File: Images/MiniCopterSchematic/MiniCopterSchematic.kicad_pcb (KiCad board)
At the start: 2 copper layers, 78.6 x 58.6 mm, 53 parts, among them J1 MPU6050, M1 Motor_DC_1, M2 Motor_DC_2, M3 Motor_DC_3, M4 Motor_DC_4, Q1 FQP20NO6L, Q2 FQP20NO6L, Q3 FQP20NO6L, Q4 FQP20NO6L

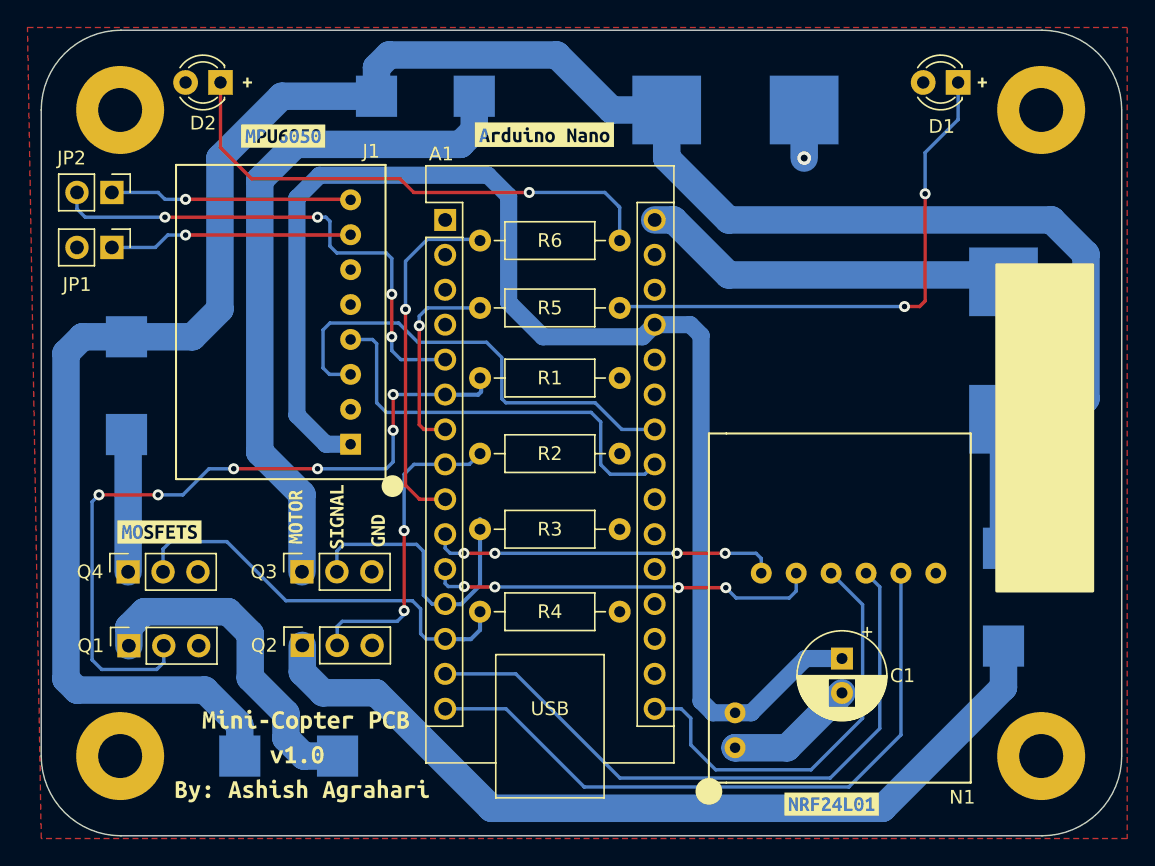
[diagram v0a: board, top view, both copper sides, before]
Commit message: Updated labels
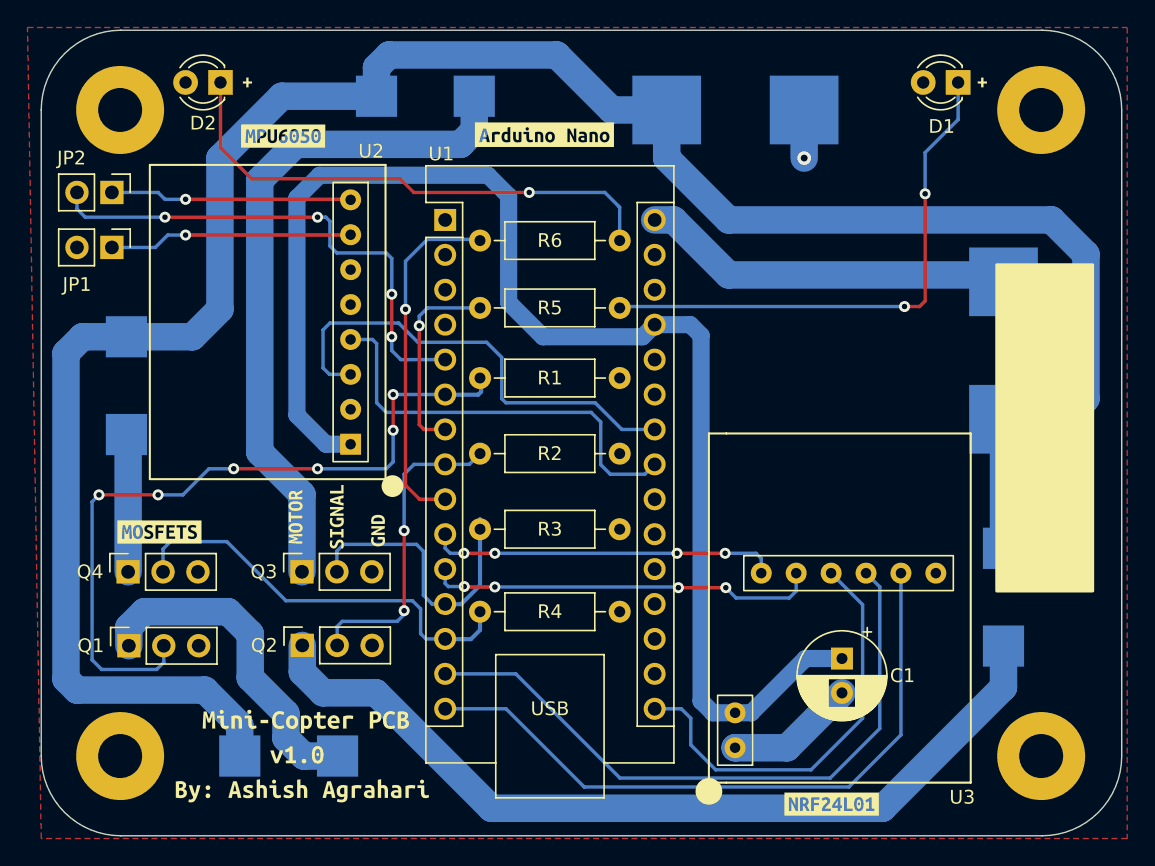
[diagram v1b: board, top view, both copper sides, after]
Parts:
- renumbered A1 to U1, J1 to U2, N1 to U3

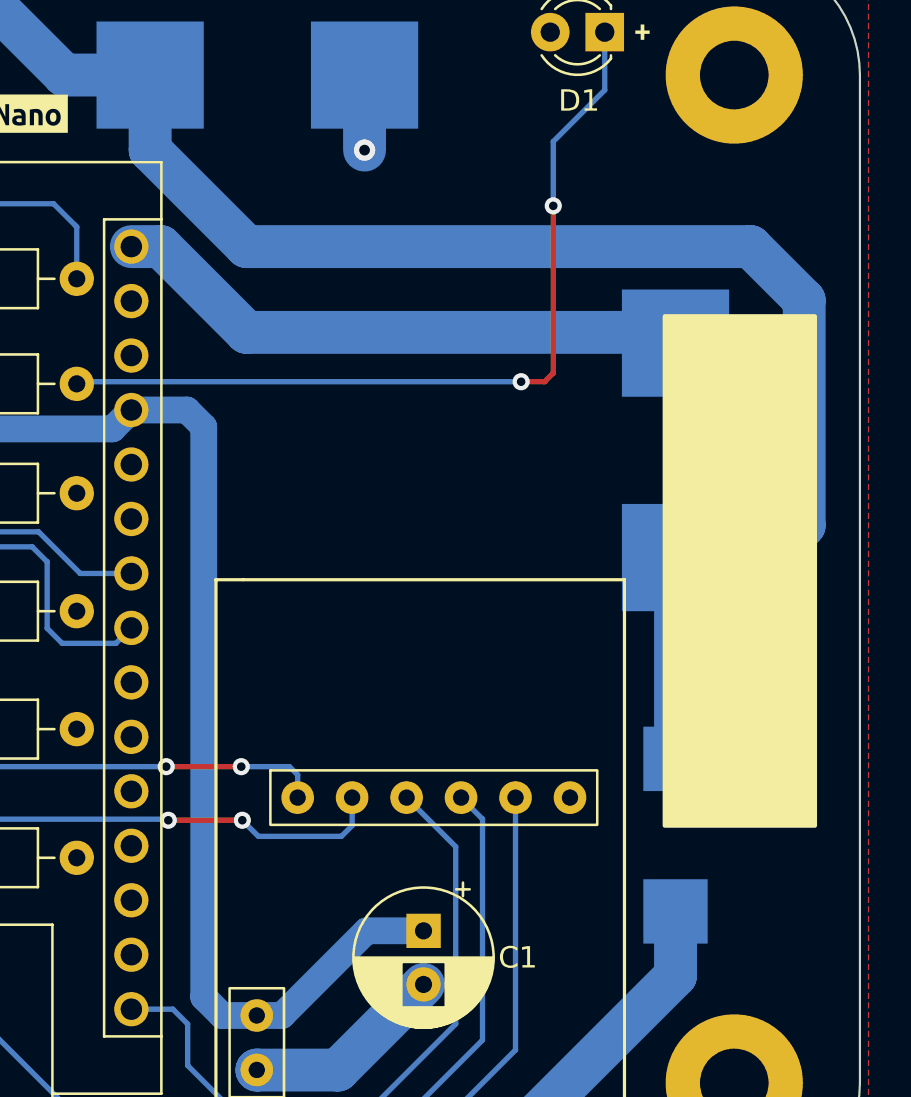
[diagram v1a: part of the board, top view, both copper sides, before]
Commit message: Added logos
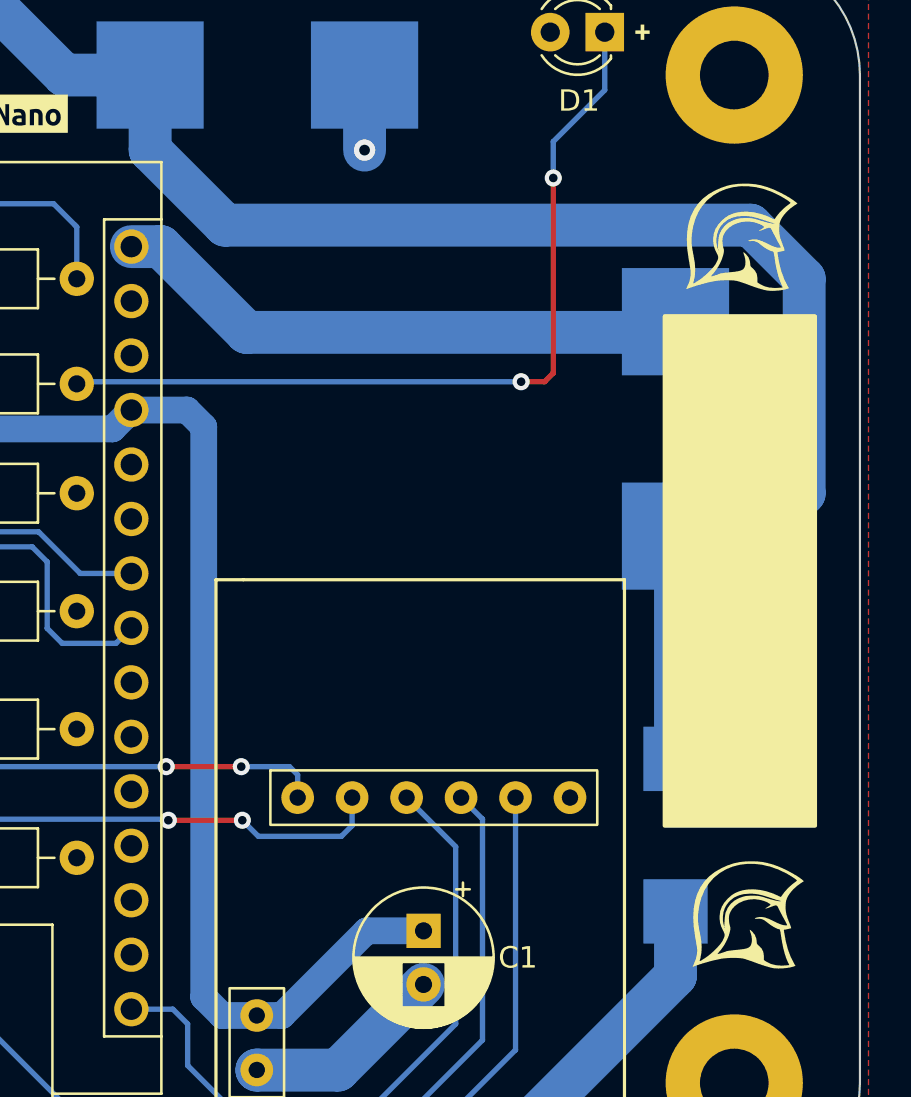
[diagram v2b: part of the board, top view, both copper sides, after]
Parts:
- added G***: LOGO, MiniCopterSchematic:FhciLogo, F.Cu at (146.5, 119.0)
- added G***: LOGO, MiniCopterSchematic:FhciLogo, F.Cu at (146.2, 87.4)
- added G***: LOGO, MiniCopterSchematic:DroneIcon, B.Cu at (129.5, 103.0)
- moved kibuzzard-64457F3E 46.1 mm to (86.5, 76.0)
- moved kibuzzard-6440BA11 1.50 mm to (138.0, 96.5)
- moved L1 1.00 mm to (143.0, 96.5)
- moved kibuzzard-6440B803 1.00 mm to (143.0, 105.5)
- moved kibuzzard-6440B80B 1.00 mm to (143.0, 87.0)

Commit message: PCB design finalizing
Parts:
- removed kibuzzard-6440AF37: G***, kibuzzard-6440AF37
- removed kibuzzard-6440AFC4: G***, kibuzzard-6440AFC4
- removed kibuzzard-6440AFCF: G***, kibuzzard-6440AFCF
- removed the kibuzzard-6440B803 at (133.5, 80.0)
- removed the kibuzzard-6440B803 at (143.0, 105.5)
- removed the kibuzzard-6440B80B at (143.0, 87.0)
- removed the kibuzzard-6440B80B at (114.0, 80.0)
- removed kibuzzard-6440BA02: G***, kibuzzard-6440BA02
- removed kibuzzard-6440BA11: G***, kibuzzard-6440BA11
- removed kibuzzard-6440EF4B: G***, kibuzzard-6440EF4B
- removed kibuzzard-64457F3E: G***, kibuzzard-64457F3E
- removed kibuzzard-644C8A62: G***, kibuzzard-644C8A62
- added G***: LOGO, MiniCopterSchematic:DroneIcon, F.Cu at (132.4, 92.5)
- added kibuzzard-644F1527: G***, kibuzzard-644F1527, F.Cu at (89.5, 82.0)
- added kibuzzard-644F152E: G***, kibuzzard-644F152E, F.Cu at (110.0, 82.0)
- added kibuzzard-644F156A: G***, kibuzzard-644F156A, F.Cu at (91.5, 128.0)
- added kibuzzard-644F15D5: G***, kibuzzard-644F15D5, F.Cu at (81.6, 110.0)
- added kibuzzard-644F167C: G***, kibuzzard-644F167C, F.Cu at (132.7, 130.5)
- added kibuzzard-644F1760: G***, kibuzzard-644F1760, B.Cu at (134.5, 130.0)
- added kibuzzard-644F1CFC: G***, kibuzzard-644F1CFC, B.Cu at (139.0, 96.0)
- added kibuzzard-644F1D01: G***, kibuzzard-644F1D01, B.Cu at (125.5, 85.0)
- added kibuzzard-644F1F4C: G***, kibuzzard-644F1F4C, F.Cu at (116.0, 80.0)
- added kibuzzard-644F1F53: G***, kibuzzard-644F1F53, F.Cu at (134.5, 80.0)
- added kibuzzard-644F1F59: G***, kibuzzard-644F1F59, F.Cu at (144.0, 86.5)
- added kibuzzard-644F1F5E: G***, kibuzzard-644F1F5E, F.Cu at (144.0, 105.0)
- moved L2 2.00 mm to (125.5, 80.0)
- moved U3 1.25 mm to (134.3, 108.6)
- moved L1 1.12 mm to (144.0, 96.0)
- moved kibuzzard-6440B80B 1.12 mm to (144.0, 108.5)
- moved M2 1.00 mm to (144.0, 115.4)
- moved kibuzzard-6440B803 1.00 mm to (144.0, 122.0)
- moved G*** 0.94 mm to (147.0, 118.2)
- moved G*** 0.65 mm to (146.8, 87.4)
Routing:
- net +BATT: track 165.7 -> 167.0 mm
- net CE_NANO: track 25.4 -> 26.7 mm
- net CSN_NANO: track 28.5 -> 29.8 mm
- net GND: track 12.9 -> 11.7 mm
- net Net-(M2-Pad2): track 63.7 -> 64.4 mm
- net +3V3: track 27.0 -> 27.6 mm
- net MISO_NANO: track 48.8 -> 49.4 mm
- net SCK_NANO: track 31.2 -> 30.6 mm

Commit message: Finalizing PCB
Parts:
- removed kibuzzard-644C468F: G***, kibuzzard-644C468F
- removed kibuzzard-644C469B: G***, kibuzzard-644C469B
- added kibuzzard-644F2052: G***, kibuzzard-644F2052, F.Cu at (135.2, 124.1)
- added kibuzzard-644F2068: G***, kibuzzard-644F2068, F.Cu at (141.5, 78.0)
- added kibuzzard-644F2071: G***, kibuzzard-644F2071, F.Cu at (88.0, 78.0)
- moved C1 6.18 mm to (137.0, 122.2), turned to 90 degrees
- moved kibuzzard-644F15D5 0.29 mm to (81.8, 110.2)
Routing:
- net CE_NANO: track 26.7 -> 39.4 mm
- net +5V: track 99.6 -> 108.7 mm
- net CSN_NANO: track 29.8 -> 37.5 mm, vias 4 -> 6
- net GND: track 11.7 -> 19.3 mm
- net MISO_NANO: track 49.4 -> 44.8 mm, vias 0 -> 2
- net MOSI_NANO: track 47.7 -> 45.8 mm, vias 0 -> 2
- net SCK_NANO: track 30.6 -> 30.9 mm, vias 0 -> 2

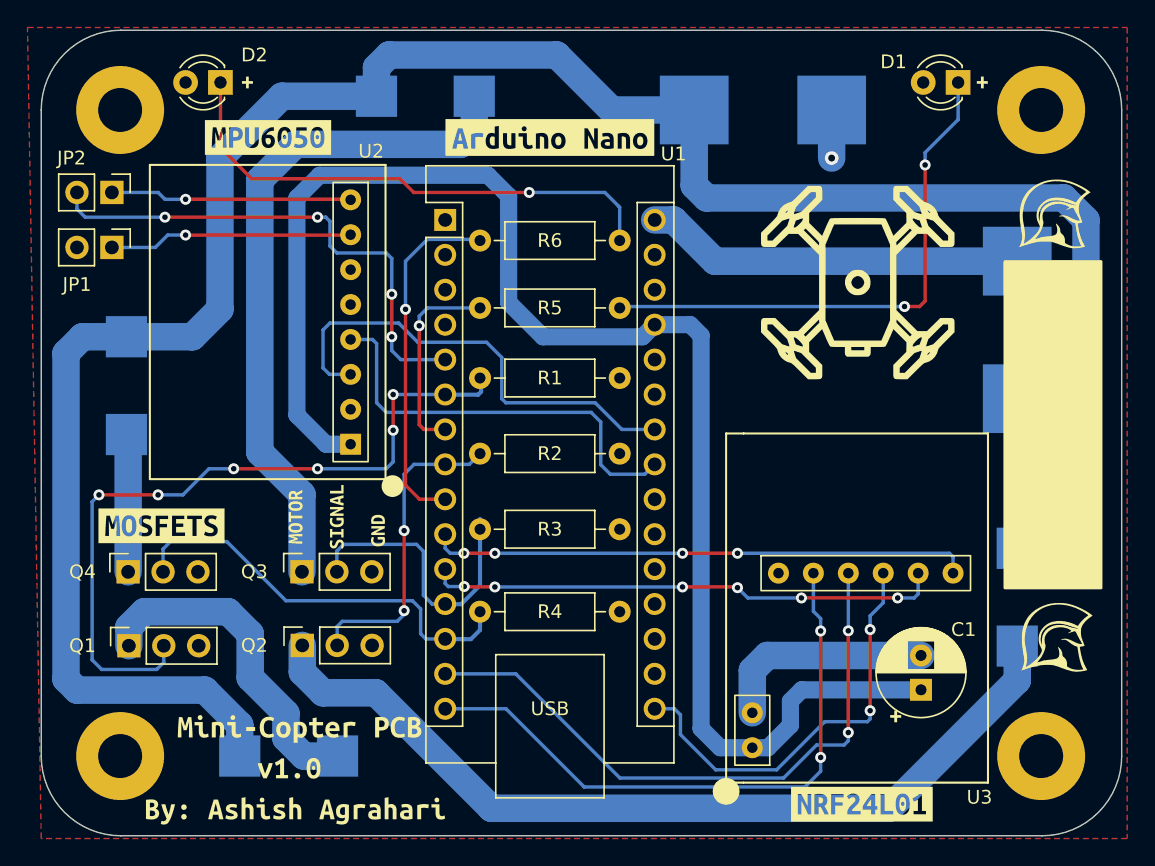
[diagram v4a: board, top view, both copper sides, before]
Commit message: Fixed mosfet pinouts
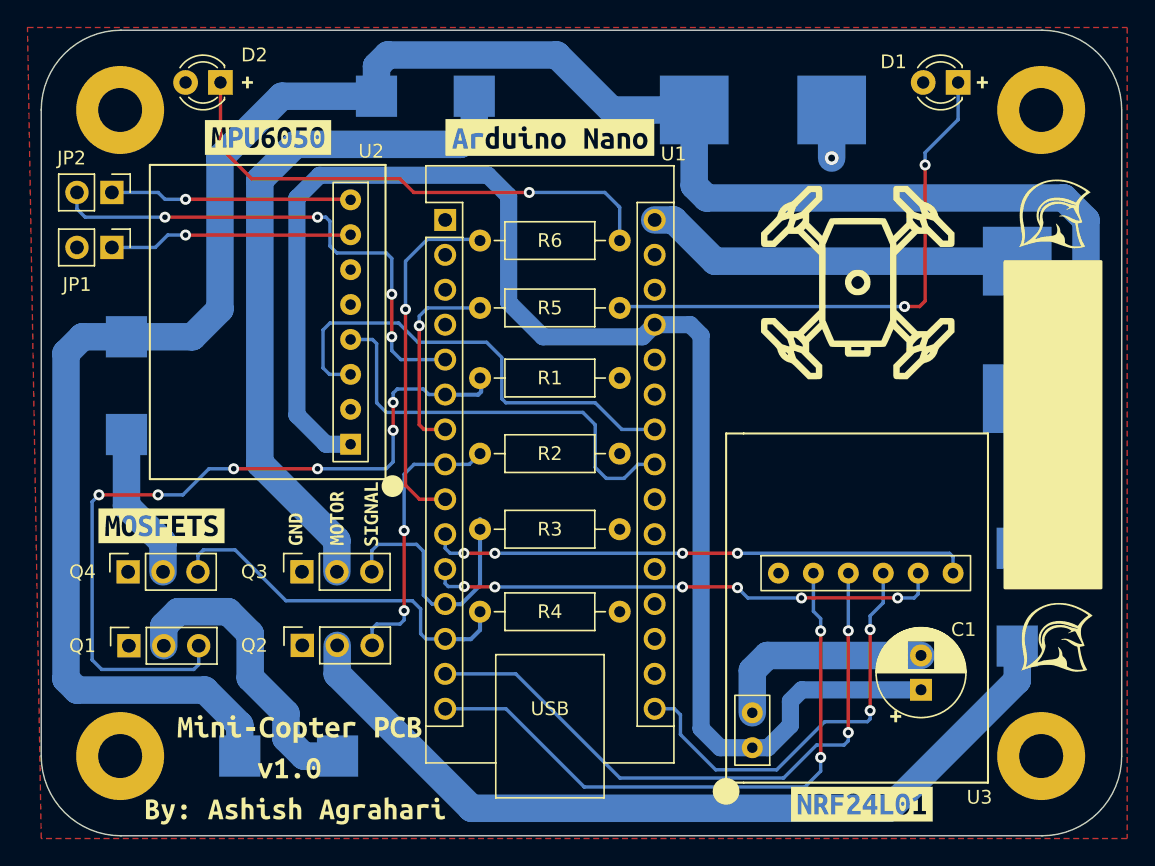
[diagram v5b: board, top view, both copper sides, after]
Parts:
- removed kibuzzard-644F1760: G***, kibuzzard-644F1760
- moved kibuzzard-6440D5EF 6.00 mm to (91.5, 110.5)
- moved kibuzzard-6440D635 3.00 mm to (94.5, 109.7)
- moved kibuzzard-6440D61E 2.51 mm to (97.0, 109.4)
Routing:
- net MOTOR_4: track 30.5 -> 27.2 mm
- net MOTOR_1: track 53.9 -> 56.9 mm
- net MOTOR_3: track 21.1 -> 18.6 mm
- net Net-(M1-Pad2): track 24.3 -> 21.8 mm
- net Net-(M2-Pad2): track 64.4 -> 61.9 mm
- net MOTOR_2: track 23.0 -> 20.6 mm
- net Net-(M4-Pad2): track 10.0 -> 11.1 mm
- net Net-(M3-Pad2): track 49.4 -> 50.4 mm
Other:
- board text added: "JLCJLCJLCJLC"

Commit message: Finalized PCB
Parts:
- moved R6 0.20 mm to (104.9, 89.3)
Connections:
- Q1 pad 1: Net-(M1-Pad2) -> MOTOR_1
- Q1 pad 2: MOTOR_1 -> Net-(M1-Pad2)
- Q2 pad 1: Net-(M2-Pad2) -> MOTOR_2
- Q2 pad 2: MOTOR_2 -> Net-(M2-Pad2)
- Q3 pad 1: Net-(M3-Pad2) -> MOTOR_3
- Q3 pad 2: MOTOR_3 -> Net-(M3-Pad2)
- Q4 pad 1: Net-(M4-Pad2) -> MOTOR_4
- Q4 pad 2: MOTOR_4 -> Net-(M4-Pad2)
